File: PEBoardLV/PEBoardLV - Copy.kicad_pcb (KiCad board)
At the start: 2 copper layers, 113.7 x 78.7 mm, 65 parts, among them J1 BSPD Test Jumper, J10 SWD Header, J11 ECU Debug Connector, J12 Extra Pin Header, J13 To TSAL, J2 Beam Interlock, J3 To HV Interlocks, J4 To Left Panel, J5 To Right Panel, J6 To Brake Light, J7 To PE HV, J8 BSPD Reset, J9 Main LV Connector, U1 MCP6004, U10 ISO1050, U11 STM32F405, U2 4072, U3 4071, U4 DE1A1B-L2-12V, U5 74HC595, U6 LM555N, U7 SN754410, U8 NCP1117DT33RKG, U9 L78S05CV-DG, Y1 8MHz

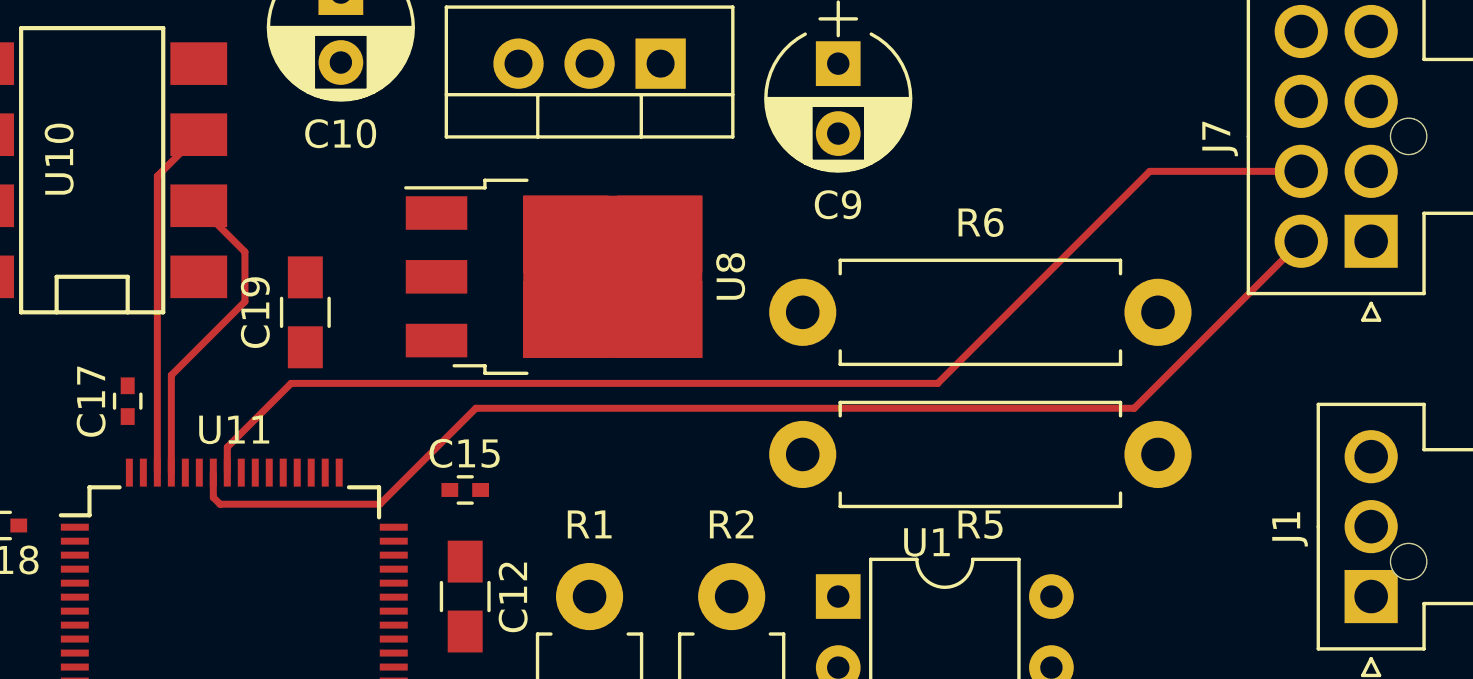
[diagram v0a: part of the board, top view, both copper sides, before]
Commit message: Route V1.0 ECU PCB, should be ready to send for manufacturing
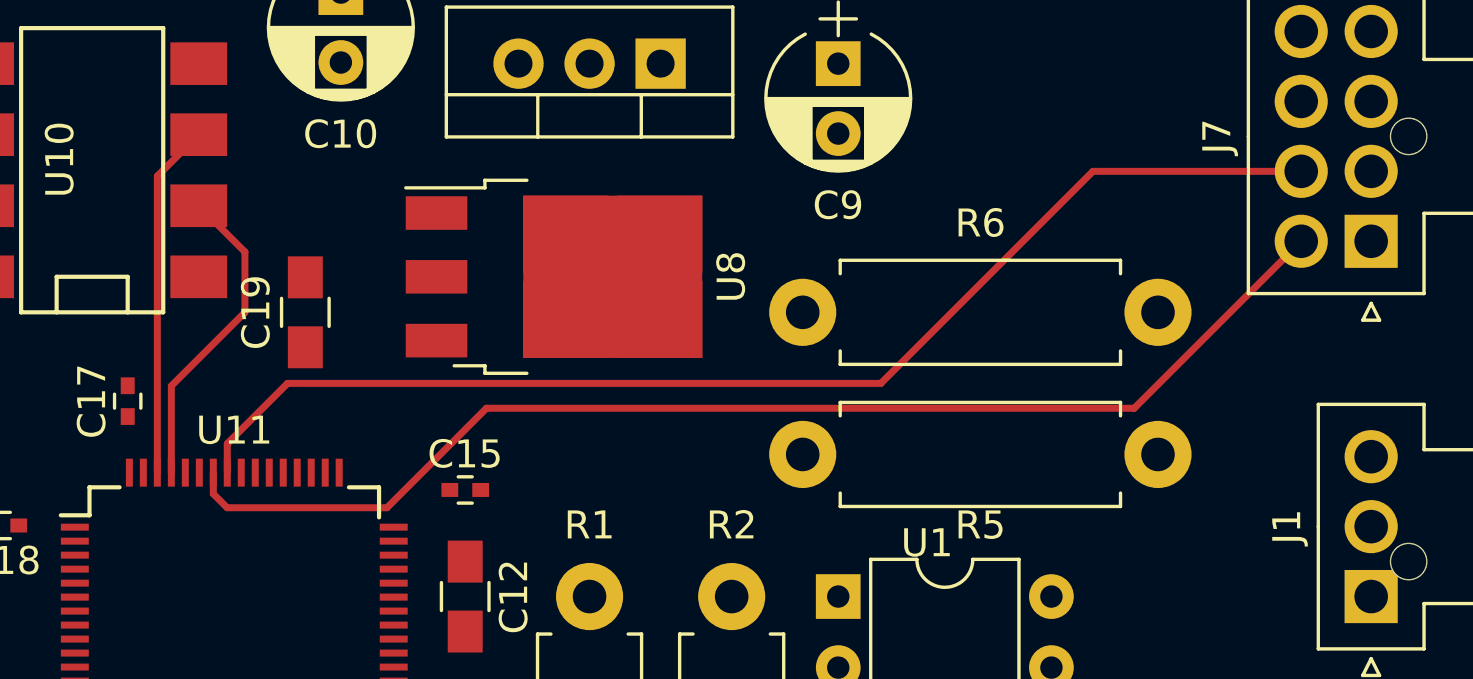
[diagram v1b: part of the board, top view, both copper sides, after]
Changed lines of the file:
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@@
     (effects (font (size 1.5 1.5) (thickness 0.3)))
   )
-  (segment (start 117.36 59.07) (end 117.36 59.956) (width 0.25) (layer F.Cu) (net 29) (status 400000))
+  (segment (start 117.36 59.07) (end 117.36 59.829) (width 0.25) (layer F.Cu) (net 29) (status 400000))
   (segment (start 150.281 56.769) (end 156.25 50.8) (width 0.25) (layer F.Cu) (net 29) (status 800000))
-  (segment (start 126.746 56.769) (end 150.281 56.769) (width 0.25) (layer F.Cu) (net 29))
-  (segment (start 123.317 60.198) (end 126.746 56.769) (width 0.25) (layer F.Cu) (net 29))
-  (segment (start 117.602 60.198) (end 123.317 60.198) (width 0.25) (layer F.Cu) (net 29))
-  (segment (start 117.36 59.956) (end 117.602 60.198) (width 0.25) (layer F.Cu) (net 29))
-  (segment (start 117.86 59.07) (end 117.86 58.162) (width 0.25) (layer F.Cu) (net 30) (status 400000))
-  (segment (start 150.836 48.3) (end 156.25 48.3) (width 0.25) (layer F.Cu) (net 30) (status 800000))
-  (segment (start 143.256 55.88) (end 150.836 48.3) (width 0.25) (layer F.Cu) (net 30))
-  (segment (start 120.142 55.88) (end 143.256 55.88) (width 0.25) (layer F.Cu) (net 30))
-  (segment (start 117.86 58.162) (end 120.142 55.88) (width 0.25) (layer F.Cu) (net 30))
-  (segment (start 115.86 59.07) (end 115.86 55.59) (width 0.25) (layer F.Cu) (net 64) (status 400000))
-  (segment (start 118.491 51.181) (end 116.84 49.53) (width 0.25) (layer F.Cu) (net 64) (status 800000))
-  (segment (start 118.491 52.959) (end 118.491 51.181) (width 0.25) (layer F.Cu) (net 64))
-  (segment (start 115.86 55.59) (end 118.491 52.959) (width 0.25) (layer F.Cu) (net 64))
-  (segment (start 115.36 59.07) (end 115.36 48.47) (width 0.25) (layer F.Cu) (net 65) (status 400000))
-  (segment (start 115.36 48.47) (end 116.84 46.99) (width 0.25) (layer F.Cu) (net 65) (status 800000))
+  (segment (start 127.127 56.769) (end 150.281 56.769) (width 0.25) (layer F.Cu) (net 29))
+  (segment (start 123.571 60.325) (end 127.127 56.769) (width 0.25) (layer F.Cu) (net 29))
+  (segment (start 117.856 60.325) (end 123.571 60.325) (width 0.25) (layer F.Cu) (net 29))
+  (segment (start 117.36 59.829) (end 117.856 60.325) (width 0.25) (layer F.Cu) (net 29))
+  (segment (start 117.86 59.07) (end 117.86 58.035) (width 0.25) (layer F.Cu) (net 30) (status 400000))
+  (segment (start 148.804 48.3) (end 156.25 48.3) (width 0.25) (layer F.Cu) (net 30) (status 800000))
+  (segment (start 141.224 55.88) (end 148.804 48.3) (width 0.25) (layer F.Cu) (net 30))
+  (segment (start 120.015 55.88) (end 141.224 55.88) (width 0.25) (layer F.Cu) (net 30))
+  (segment (start 117.86 58.035) (end 120.015 55.88) (width 0.25) (layer F.Cu) (net 30))
+  (segment (start 115.86 59.07) (end 115.86 55.971) (width 0.25) (layer F.Cu) (net 64))
+  (segment (start 118.491 51.181) (end 116.84 49.53) (width 0.25) (layer F.Cu) (net 64))
+  (segment (start 118.491 53.34) (end 118.491 51.181) (width 0.25) (layer F.Cu) (net 64))
+  (segment (start 115.86 55.971) (end 118.491 53.34) (width 0.25) (layer F.Cu) (net 64))
+  (segment (start 115.36 59.07) (end 115.36 48.47) (width 0.25) (layer F.Cu) (net 65))
+  (segment (start 115.36 48.47) (end 116.84 46.99) (width 0.25) (layer F.Cu) (net 65))
 )
